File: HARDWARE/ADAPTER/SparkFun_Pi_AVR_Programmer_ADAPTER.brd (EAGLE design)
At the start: 15.2 x 31.8 mm, 5 parts, among them J1 AVR 3X2 TARGET, J2 CABLE

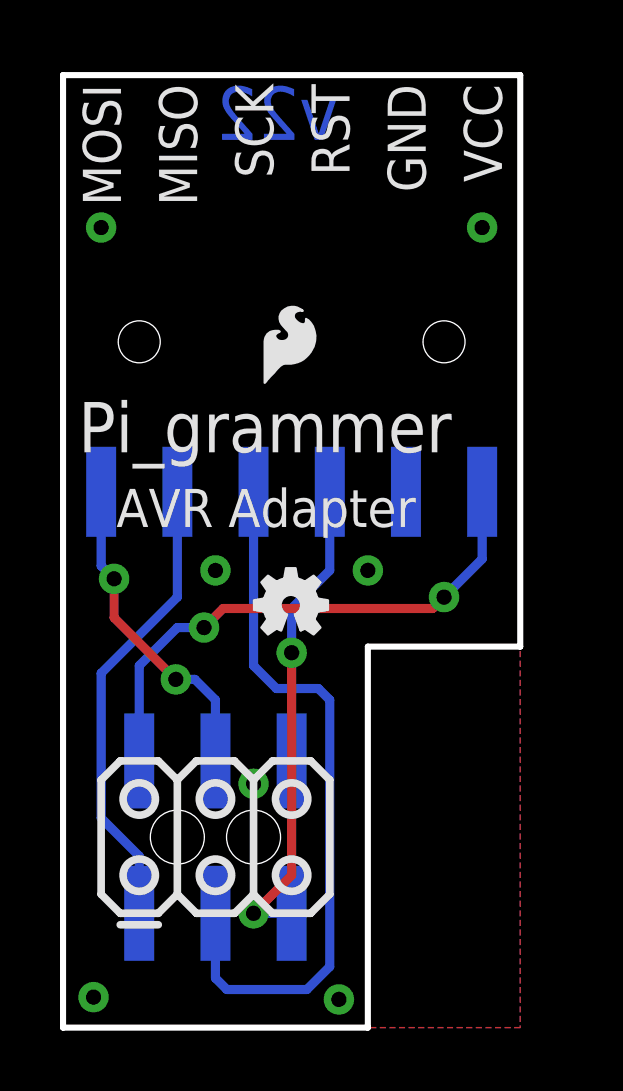
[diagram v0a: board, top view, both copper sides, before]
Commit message: Adjusted silk for new product name
Also updated all silk to sweet buzzard style labels
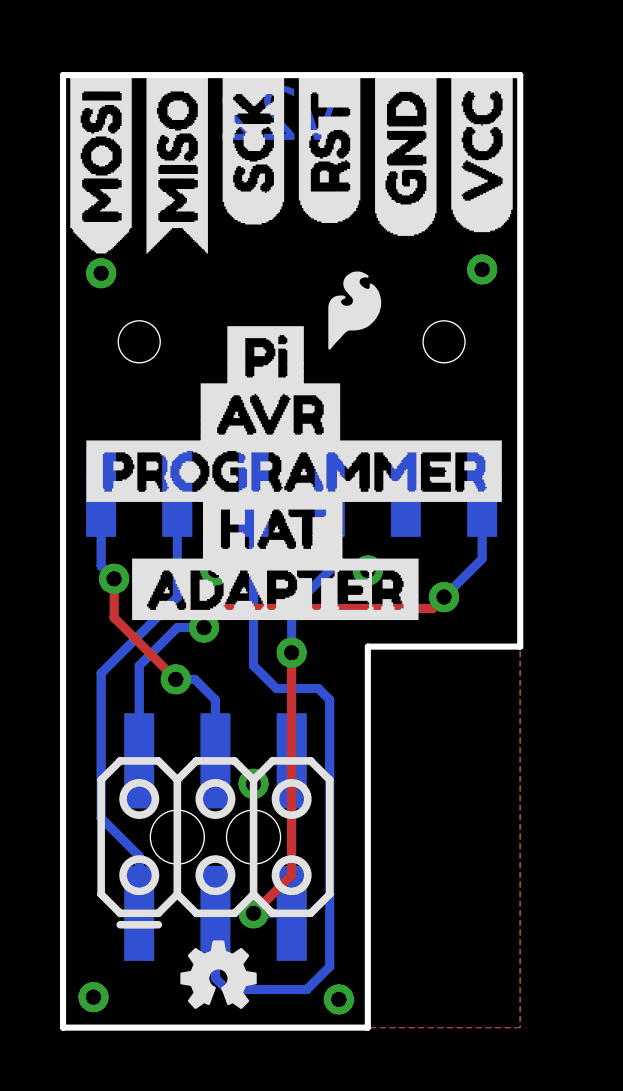
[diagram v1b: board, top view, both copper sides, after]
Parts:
- added U$1: (no value), buzzard_labels (10):GND1
- added U$10: (no value), buzzard_labels (11):HAT3
- added U$11: (no value), buzzard_labels (11):ADAPTER4
- added U$2: (no value), buzzard_labels (10):MISO5
- added U$3: (no value), buzzard_labels (10):MOSI4
- added U$4: (no value), buzzard_labels (10):RST2
- added U$5: (no value), buzzard_labels (10):SCK3
- added U$6: (no value), buzzard_labels (10):VCC0
- added U$7: (no value), buzzard_labels (11):PI0
- added U$8: (no value), buzzard_labels (11):AVR1
- added U$9: (no value), buzzard_labels (11):PROGRAMMER2
- moved LOGO2 12.7 mm to (5.18, 1.65)
- moved LOGO1 2.44 mm to (8.56, 22.3)
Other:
- board text removed: "AVR Adapter"
- board text removed: "Pi_grammer"
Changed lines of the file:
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@@
 <setting verticaltext="up"/>
 </settings>
-<grid distance="0.05" unitdist="inch" unit="inch" style="lines" multiple="1" display="yes" altdistance="0.001" altunitdist="inch" altunit="inch"/>
+<grid distance="0.05" unitdist="inch" unit="inch" style="lines" multiple="1" display="yes" altdistance="0.005" altunitdist="inch" altunit="inch"/>
 <layers>
 <layer number="1" name="Top" color="4" fill="1" visible="yes" active="yes"/>
@@
 <text x="8.89" y="-12.7" size="1.778" layer="51" font="vector">Pete Lewis</text>
 <text x="5.08" y="30.48" size="1.778" layer="16" font="vector" ratio="21" rot="MR0" align="center-right">v22</text>
-<text x="1.2954" y="31.4452" size="1.27" layer="21" font="vector" ratio="15" rot="R90" align="center-right">MOSI</text>
-<text x="3.8354" y="31.4452" size="1.27" layer="21" font="vector" ratio="15" rot="R90" align="center-right">MISO</text>
-<text x="6.3754" y="31.4452" size="1.27" layer="21" font="vector" ratio="15" rot="R90" align="center-right">SCK</text>
-<text x="8.9154" y="31.4452" size="1.27" layer="21" font="vector" ratio="15" rot="R90" align="center-right">RST</text>
-<text x="11.4554" y="31.4452" size="1.27" layer="21" font="vector" ratio="15" rot="R90" align="center-right">GND</text>
-<text x="13.9954" y="31.4452" size="1.27" layer="21" font="vector" ratio="15" rot="R90" align="center-right">VCC</text>
 <wire x1="3.81" y1="8.255" x2="3.175" y2="8.89" width="0.254" layer="21"/>
 <wire x1="3.175" y1="8.89" x2="1.905" y2="8.89" width="0.254" layer="21"/>
@@
 <text x="8.763" y="9.144" size="0.8128" layer="22" font="vector" ratio="15" rot="MR270" align="center-right">GND</text>
 <text x="3.683" y="9.144" size="0.8128" layer="22" font="vector" ratio="15" rot="MR270" align="center-right">VCC</text>
-<text x="0.508" y="19.177" size="1.6764" layer="21" font="vector" ratio="15">Pi_grammer</text>
-<text x="1.778" y="16.6878" size="1.27" layer="21" font="vector" ratio="15">AVR Adapter</text>
 </plain>
 <attributes>
@@
 <attribute name="PROD_ID" value="CONN-11415" x="5.08" y="6.35" size="1.778" layer="28" font="vector" ratio="15" rot="MR180" display="off"/>
 </element>
-<element name="LOGO1" library="SparkFun-Aesthetics" package="SFE_LOGO_FLAME_.1" value="SFE_LOGO_FLAME.1_INCH" x="6.4008" y="21.1328"/>
-<element name="LOGO2" library="SparkFun-Aesthetics" package="OSHW-LOGO-MINI" value="OSHW-LOGOMINI" x="7.5946" y="14.097"/>
+<element name="LOGO1" library="SparkFun-Aesthetics" package="SFE_LOGO_FLAME_.1" value="SFE_LOGO_FLAME.1_INCH" x="8.5598" y="22.2758"/>
+<element name="LOGO2" library="SparkFun-Aesthetics" package="OSHW-LOGO-MINI" value="OSHW-LOGOMINI" x="5.1816" y="1.651"/>
+<element name="U$1" library="buzzard_labels (10)" package="GND1" value="" x="11.43" y="26.289" rot="R90"/>
+<element name="U$2" library="buzzard_labels (10)" package="MISO5" value="" x="3.81" y="25.654" rot="R90"/>
+<element name="U$3" library="buzzard_labels (10)" package="MOSI4" value="" x="1.27" y="25.654" rot="R90"/>
+<element name="U$4" library="buzzard_labels (10)" package="RST2" value="" x="8.89" y="26.67" rot="R90"/>
+<element name="U$5" library="buzzard_labels (10)" package="SCK3" value="" x="6.35" y="26.67" rot="R90"/>
+<element name="U$6" library="buzzard_labels (10)" package="VCC0" value="" x="13.97" y="26.416" rot="R90"/>
+<element name="U$7" library="buzzard_labels (11)" package="PI0" value="" x="4.826" y="22.352"/>
+<element name="U$8" library="buzzard_labels (11)" package="AVR1" value="" x="3.937" y="20.447"/>
+<element name="U$9" library="buzzard_labels (11)" package="PROGRAMMER2" value="" x="0.127" y="18.542"/>
+<element name="U$10" library="buzzard_labels (11)" package="HAT3" value="" x="4.064" y="16.637"/>
+<element name="U$11" library="buzzard_labels (11)" package="ADAPTER4" value="" x="1.651" y="14.605"/>
 </elements>
 <signals>
@@
 </polygon>
 <contactref element="J1" pad="5"/>
-<via x="13.97" y="26.67" extent="1-16" drill="0.508"/>
-<via x="1.27" y="26.67" extent="1-16" drill="0.508"/>
+<via x="13.97" y="25.273" extent="1-16" drill="0.508"/>
+<via x="1.27" y="25.146" extent="1-16" drill="0.508"/>
 <via x="6.35" y="8.128" extent="1-16" drill="0.508"/>
 <via x="5.08" y="15.24" extent="1-16" drill="0.508"/>
